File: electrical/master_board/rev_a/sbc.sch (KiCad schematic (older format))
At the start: 21 parts, among them CN94 RASPI;F2X20, SW2 BUTTON;6x3.5, U2 MCP7940;SOIC8, U3 CAT24C32;SOIC8, X1 32.768kHz9pF;3.2x1.5

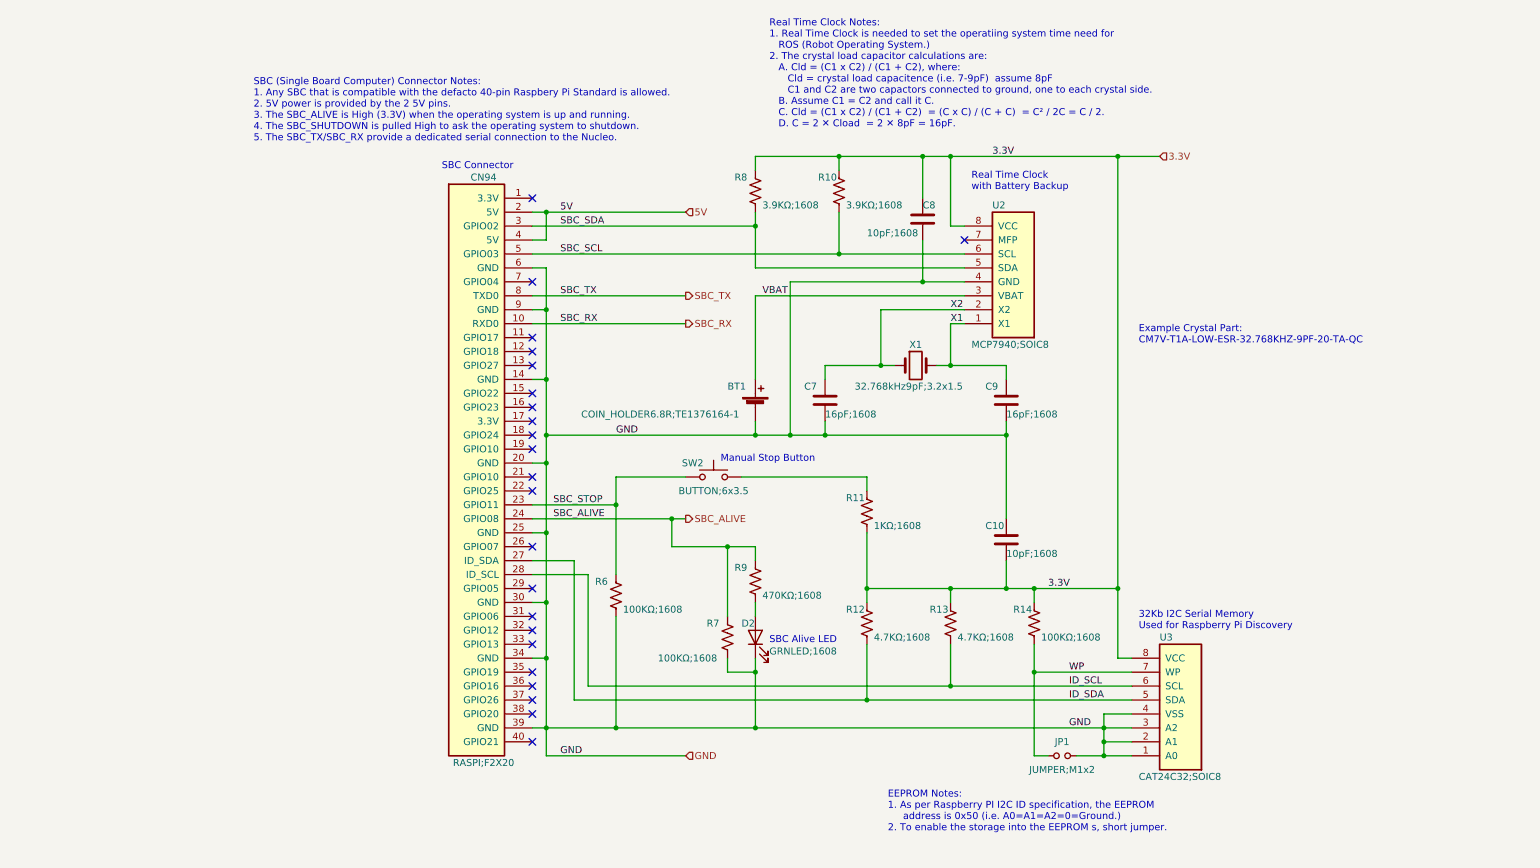
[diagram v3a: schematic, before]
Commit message: More work thinning rats nest of unconnected wires.
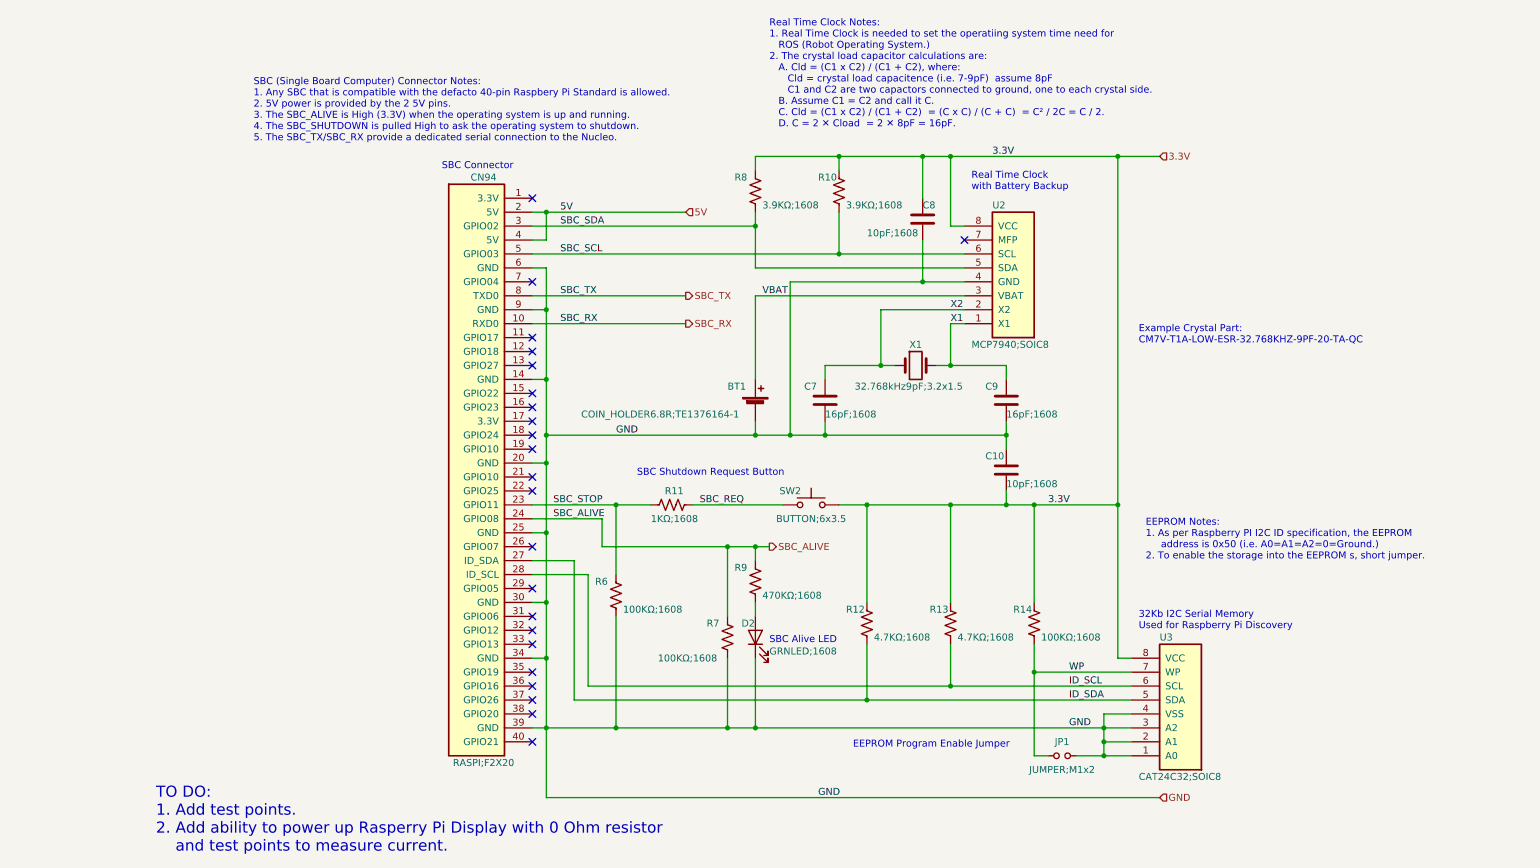
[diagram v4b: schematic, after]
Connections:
- net 3.3V: now also SW2.2; no longer R11.2
- net SBC_STOP: now also R11.2; no longer SW2.1
- net SBC_REQ: now reaches R11.1
- net SBC_REQ: now also SW2.1; no longer SW2.2
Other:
- note added: "EEPROM Program Enable Jumper"
- note added: "SBC Shutdown Request Button"
- note added: "TO DO:\n1. Add test points.\n2. Add ability to power up Rasperry Pi Display with 0 Ohm resistor\n and test points to measure current."
- note removed: "Manual Stop Button"
- moved on the sheet: C10, R11, SW2
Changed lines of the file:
@@
 	8200 5300 8100 5300
 Wire Wire Line
-	8100 5300 8100 4800
-Wire Wire Line
-	8100 4800 7500 4800
-Wire Wire Line
-	6900 4800 6900 4900
-Wire Wire Line
-	7500 4900 7500 4800
-Connection ~ 7500 4800
-Wire Wire Line
-	7500 4800 7300 4800
+	8100 5300 8100 4200
+Wire Wire Line
+	8100 4200 7500 4200
+Wire Wire Line
+	6900 4200 6900 4900
+Wire Wire Line
+	7500 4900 7500 4200
+Connection ~ 7500 4200
+Wire Wire Line
+	7500 4200 7300 4200
 $Comp
 L Device:R_US R12
@@
 $EndComp
 Wire Wire Line
-	6300 4900 6300 4800
-Wire Wire Line
-	6300 4800 6900 4800
-Connection ~ 6900 4800
+	6300 4200 6900 4200
+Connection ~ 6900 4200
 Wire Wire Line
 	8200 5400 7500 5400
@@
 Wire Wire Line
 	8000 5800 8000 5900
-Text Notes 6450 6550 0    50   ~ 0
+Text Notes 8300 4600 0    50   ~ 0
 EEPROM Notes:\n1. As per Raspberry PI I2C ID specification, the EEPROM\n     address is 0x50 (i.e. A0=A1=A2=0=Ground.)\n2. To enable the storage into the EEPROM s, short jumper.\n
 Wire Wire Line
@@
 	4000 2100 5000 2100
 Connection ~ 4000 2100
-Text HLabel 5000 6000 2    50   Input ~ 0
+Text HLabel 8400 6300 2    50   Input ~ 0
 GND
 Wire Wire Line
-	4000 5800 4000 6000
-Wire Wire Line
-	4000 6000 5000 6000
-Text Label 4100 6000 0    50   ~ 0
+	4000 5800 4000 6300
+Wire Wire Line
+	4000 6300 8400 6300
+Text Label 5950 6300 0    50   ~ 0
 GND
 Wire Wire Line
@@
 Wire Wire Line
 	8100 1700 6900 1700
-Connection ~ 8100 4800
+Connection ~ 8100 4200
 Connection ~ 6900 1700
 Text HLabel 8400 1700 2    50   Input ~ 0
@@
 Wire Wire Line
 	4000 3900 4000 4400
-Text HLabel 5000 4300 2    50   Output ~ 0
+Text HLabel 5600 4500 2    50   Output ~ 0
 SBC_ALIVE
 Wire Wire Line
@@
 Text Label 4500 3700 0    50   ~ 0
 GND
-Text Label 7600 4800 0    50   ~ 0
+Text Label 7600 4200 0    50   ~ 0
 3.3V
 Text Label 7750 5500 0    50   ~ 0
@@
 L Switch:SW_Push SW?
 U 1 1 5F8FBAFA
-P 5200 4000
+P 5900 4200
 AR Path="/5F52F39E/5F8FBAFA" Ref="SW?"  Part="1"
 AR Path="/5F4877FA/5F8FBAFA" Ref="SW2"  Part="1"
-F 0 "SW2" H 5050 4100 50  0000 C CNN
-F 1 "BUTTON;6x3.5" H 5200 3900 50  0000 C CNN
-F 2 "HR2:BUTTON_6x3.5" H 5200 4200 50  0001 C CNN
-F 3 "~" H 5200 4200 50  0001 C CNN
-	1    5200 4000
+F 0 "SW2" H 5750 4300 50  0000 C CNN
+F 1 "BUTTON;6x3.5" H 5900 4100 50  0000 C CNN
+F 2 "HR2:BUTTON_6x3.5" H 5900 4400 50  0001 C CNN
+F 3 "~" H 5900 4400 50  0001 C CNN
+	1    5900 4200
 	1    0    0    -1
 $EndComp
@@
 NoConn ~ 3900 2000
 Wire Wire Line
-	4500 4200 4500 4000
-Wire Wire Line
-	4500 4000 5000 4000
+	4500 4200 4750 4200
 $Comp
 L Device:R_US R11
 U 1 1 5FAF8B92
-P 6300 4250
+P 4900 4200
 AR Path="/5F4877FA/5FAF8B92" Ref="R11"  Part="1"
 AR Path="/5FA587FE/5FAF8B92" Ref="R?"  Part="1"
-F 0 "R11" H 6150 4350 50  0000 L CNN
-F 1 "1KΩ;1608" H 6350 4150 50  0000 L CNN
-F 2 "Resistor_SMD:R_0603_1608Metric" V 6340 4240 50  0001 C CNN
-F 3 "~" H 6300 4250 50  0001 C CNN
-	1    6300 4250
-	1    0    0    -1
-$EndComp
-Wire Wire Line
-	5400 4000 6300 4000
-Wire Wire Line
-	6300 4000 6300 4100
+F 0 "R11" V 4800 4150 50  0000 L CNN
+F 1 "1KΩ;1608" V 5000 4050 50  0000 L CNN
+F 2 "Resistor_SMD:R_0603_1608Metric" V 4940 4190 50  0001 C CNN
+F 3 "~" H 4900 4200 50  0001 C CNN
+	1    4900 4200
+	0    1    1    0
+$EndComp
+Wire Wire Line
+	5050 4200 5700 4200
 $Comp
 L Device:LED D?
@@
 $EndComp
 Wire Wire Line
-	6300 4800 6300 4400
-Connection ~ 6300 4800
-Wire Wire Line
-	4900 4300 4900 4500
-Wire Wire Line
-	4900 4500 5300 4500
+	4400 4300 4400 4500
+Wire Wire Line
+	4400 4500 5300 4500
 Wire Wire Line
 	5500 4500 5500 4600
-Connection ~ 4900 4300
-Wire Wire Line
-	4900 4300 5000 4300
 Wire Wire Line
 	5500 5000 5500 4900
-Wire Wire Line
-	5500 5300 5500 5400
 Connection ~ 5500 5800
 Wire Wire Line
-	5500 5800 4500 5800
-Text Notes 5250 3900 0    50   ~ 0
-Manual Stop Button
+	5500 5800 5300 5800
+Text Notes 4650 4000 0    50   ~ 0
+SBC Shutdown Request Button
 Text Notes 5600 5200 0    50   ~ 0
 SBC Alive LED
 Wire Wire Line
-	3900 4300 4900 4300
+	3900 4300 4400 4300
 Wire Wire Line
 	4000 5800 4500 5800
@@
 Wire Wire Line
 	5300 4500 5500 4500
-Wire Wire Line
-	5300 5300 5300 5400
-Wire Wire Line
-	5300 5400 5500 5400
-Connection ~ 5500 5400
-Wire Wire Line
-	5500 5400 5500 5800
 $Comp
 L Device:C C10
 U 1 1 5FA44A8F
-P 7300 4450
+P 7300 3950
 AR Path="/5F4877FA/5FA44A8F" Ref="C10"  Part="1"
 AR Path="/5FA587FE/5FA44A8F" Ref="C?"  Part="1"
-F 0 "C10" H 7150 4550 50  0000 L CNN
-F 1 "10pF;1608" H 7300 4350 50  0000 L CNN
-F 2 "Capacitor_SMD:C_0603_1608Metric" H 7338 4300 50  0001 C CNN
-F 3 "~" H 7300 4450 50  0001 C CNN
-	1    7300 4450
-	1    0    0    -1
-$EndComp
-Wire Wire Line
-	7300 4600 7300 4800
-Connection ~ 7300 4800
-Wire Wire Line
-	7300 4800 6900 4800
-Wire Wire Line
-	7300 4300 7300 3700
+F 0 "C10" H 7150 4050 50  0000 L CNN
+F 1 "10pF;1608" H 7300 3850 50  0000 L CNN
+F 2 "Capacitor_SMD:C_0603_1608Metric" H 7338 3800 50  0001 C CNN
+F 3 "~" H 7300 3950 50  0001 C CNN
+	1    7300 3950
+	1    0    0    -1
+$EndComp
+Connection ~ 7300 4200
+Wire Wire Line
+	7300 4200 6900 4200
+Wire Wire Line
+	7300 3800 7300 3700
 Connection ~ 7300 3700
 Text Notes 8250 3050 0    50   ~ 0
@@
 	6700 2000 6700 1700
 Wire Wire Line
-	8100 4800 8100 1700
+	8100 4200 8100 1700
 $Comp
 L Device:C C8
@@
 Wire Wire Line
 	6700 2600 7000 2600
+Text Notes 1200 6700 0    80   ~ 0
+TO DO:\n1. Add test points.\n2. Add ability to power up Rasperry Pi Display with 0 Ohm resistor\n    and test points to measure current.
+Wire Wire Line
+	5500 4500 5600 4500
+Connection ~ 5500 4500
+Wire Wire Line
+	6300 4200 6300 4900
+Wire Wire Line
+	6100 4200 6300 4200
+Connection ~ 6300 4200
+Wire Wire Line
+	7300 4100 7300 4200
+Connection ~ 5300 5800
+Wire Wire Line
+	5300 5800 4500 5800
+Text Notes 6200 5950 0    50   ~ 0
+EEPROM Program Enable Jumper
+Wire Wire Line
+	5300 5300 5300 5800
+Wire Wire Line
+	5500 5300 5500 5800
+Text Label 5100 4200 0    50   ~ 0
+SBC_REQ
 $EndSCHEMATC

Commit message: More work on raspi display electronics.
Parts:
- added JP?: Jumper_3_Open, symbol Jumper:Jumper_3_Open
- added Q?: POWER_PFET_GSD, Package_TO_SOT_SMD:SOT-23, symbol HR2:POWER_PFET_GSD
- added R? (x2): 3.9KΩ;1608, Resistor_SMD:R_0603_1608Metric, symbol Device:R_US
- added TP?: TestPoint, symbol Connector:TestPoint
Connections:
- wire segments 118 -> 128
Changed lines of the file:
@@
 Text Label 5100 4200 0    50   ~ 0
 SBC_REQ
+$Comp
+L Connector:TestPoint TP?
+U 1 1 5FB4ED7C
+P 8600 3700
+F 0 "TP?" H 8658 3818 50  0000 L CNN
+F 1 "TestPoint" H 8658 3727 50  0000 L CNN
+F 2 "" H 8800 3700 50  0001 C CNN
+F 3 "~" H 8800 3700 50  0001 C CNN
+	1    8600 3700
+	1    0    0    -1
+$EndComp
+$Comp
+L HR2:POWER_PFET_GSD Q?
+U 1 1 5FB5982B
+P 2050 2300
+AR Path="/5F52F39E/5FB5982B" Ref="Q?"  Part="1"
+AR Path="/5F4877FA/5FB5982B" Ref="Q?"  Part="1"
+F 0 "Q?" H 2300 2450 50  0000 C CNN
+F 1 "POWER_PFET_GSD" H 2450 2050 50  0000 C CNN
+F 2 "Package_TO_SOT_SMD:SOT-23" H 2250 2350 60  0001 L CNN
+F 3 "Power PFG (GSD pinout)" H 2250 2150 60  0001 L CNN
+F 4 "Power PFET (GSD pinout)" H 2250 2050 60  0001 L CNN "Field5"
+	1    2050 2300
+	1    0    0    -1
+$EndComp
+Wire Wire Line
+	4000 2100 4000 1650
+Wire Wire Line
+	4000 1650 1950 1650
+Wire Wire Line
+	1950 1650 1950 2300
+Wire Wire Line
+	1950 2300 2050 2300
+$Comp
+L Jumper:Jumper_3_Open JP?
+U 1 1 5FB67673
+P 1400 2150
+F 0 "JP?" H 1400 2374 50  0000 C CNN
+F 1 "Jumper_3_Open" H 1400 2283 50  0000 C CNN
+F 2 "" H 1400 2150 50  0001 C CNN
+F 3 "~" H 1400 2150 50  0001 C CNN
+	1    1400 2150
+	1    0    0    -1
+$EndComp
+$Comp
+L Device:R_US R?
+U 1 1 5FB68DCD
+P 1000 2400
+AR Path="/5F4877FA/5FB68DCD" Ref="R?"  Part="1"
+AR Path="/5FA587FE/5FB68DCD" Ref="R?"  Part="1"
+F 0 "R?" H 850 2500 50  0000 L CNN
+F 1 "3.9KΩ;1608" H 1050 2300 50  0000 L CNN
+F 2 "Resistor_SMD:R_0603_1608Metric" V 1040 2390 50  0001 C CNN
+F 3 "~" H 1000 2400 50  0001 C CNN
+	1    1000 2400
+	1    0    0    -1
+$EndComp
+$Comp
+L Device:R_US R?
+U 1 1 5FB69F2A
+P 1750 1900
+AR Path="/5F4877FA/5FB69F2A" Ref="R?"  Part="1"
+AR Path="/5FA587FE/5FB69F2A" Ref="R?"  Part="1"
+F 0 "R?" H 1600 2000 50  0000 L CNN
+F 1 "3.9KΩ;1608" H 1800 1800 50  0000 L CNN
+F 2 "Resistor_SMD:R_0603_1608Metric" V 1790 1890 50  0001 C CNN
+F 3 "~" H 1750 1900 50  0001 C CNN
+	1    1750 1900
+	1    0    0    -1
+$EndComp
+Wire Wire Line
+	1650 2150 1750 2150
+Wire Wire Line
+	1750 2150 1750 2050
+Wire Wire Line
+	1750 1750 1750 1650
+Wire Wire Line
+	1750 1650 1950 1650
+Connection ~ 1950 1650
+Wire Wire Line
+	1150 2150 1000 2150
+Wire Wire Line
+	1000 2150 1000 2250
 $EndSCHEMATC
